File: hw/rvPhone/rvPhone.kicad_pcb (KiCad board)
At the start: 4 copper layers, 126 x 68 mm, 262 parts, among them J1 USB_OTG, J2 BATT, J201 Modem, J202 SIM_Card, J203 Motor, J204 Micro_SD_Card_Det, J205 Prog, J206 Expansion, J207 Camera, J3 +5V, J301 iMX8, J302 Micro_SD_Card_Det, J303 Spacer, J4 SJ-3571N, J401 Display, J402 Spacer, J403 Spacer, J5 SPEAKER, SW1 RESET, SW2 WAKE, SW201 ESP32_RST, SW202 MODEM_RST, SW301 iMX8_ALT_BOOT, SW302 iMX8_RST, SW303 iMX8_PWR, U1 BQ25895, U10 74HC595, U11 ICS-43434, U12 MAX98357A, U13 MAX98357A, U14 SN74LVC1G04DCK, U15 SN74LVC1G3157DCK, U16 SN74LVC2G07DCK, U2 TPS62293, U201 ESP32-WROOM, U202 SN74CBTLV3125RGY, U203 TXB0104RGY, U204 TXB0104RGY, U205 DRV2605LDGS, U206 LSM9DS1, U207 FT230XQ, U208 TMUX154ERSW, U3 TPS630250, U4 FE310-G002, U401 FAN5333BSX, U402 SN74LVC3G06DCU, U403 BT817Q, U404 IS25LP128-JKLE, U405 DS90C185, U406 TS3DV520ERUA, U407 TMUX1574RSV, U5 IS25LP128-JKLE, U6 TMUX1574RSV, U7 74HC00, U8 74HC00, U9 74HC595, X1 SiT1533, Y1 16MHz, Y401 12MHz

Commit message: HW REV 3.0
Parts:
- removed the C42 at (111.3, 135.4)
- removed the C43 at (108.0, 134.8)
- removed the C44 at (108.0, 132.8)
- removed the R31 at (163.8, 106.3)
- removed TP1: BQ_INT, TestPoint:TestPoint_Pad_D1.5mm
- removed TP401: AUDIO, TestPoint:TestPoint_Pad_D1.5mm
- added C39: 0.1uF, Capacitor_SMD:C_0603_1608Metric, B.Cu at (218.2, 121.0)
- added C40: 0.1uF, Capacitor_SMD:C_0603_1608Metric, B.Cu at (218.2, 124.0)
- added C45: 0.1uF, Capacitor_SMD:C_0603_1608Metric, B.Cu at (230.0, 117.0)
- added C50: 10uF, Capacitor_SMD:C_0603_1608Metric, F.Cu at (117.2, 136.6)
- added C51: 22uF, Capacitor_SMD:C_0805_2012Metric, F.Cu at (109.2, 135.4)
- added C52: 22uF, Capacitor_SMD:C_0805_2012Metric, F.Cu at (107.2, 135.4)
- added C53: 10uF, Capacitor_SMD:C_0603_1608Metric, F.Cu at (112.5, 133.4)
- added C54: 10uF, Capacitor_SMD:C_0603_1608Metric, F.Cu at (111.0, 133.4)
- added C9: 10uF, Capacitor_SMD:C_0603_1608Metric, F.Cu at (130.6, 122.7)
- added D2: LED, LED_SMD:LED_0603_1608Metric, B.Cu at (117.7, 138.3)
- added J6: Ext Audio, Connector_Molex:Molex_SlimStack_54722-0164_2x08_P0.50mm_Vertical, F.Cu at (228.2, 122.7)
- added JP1: AUDIO PWR, Jumper:SolderJumper-3_P1.3mm_Open_RoundedPad1.0x1.5mm, B.Cu at (162.1, 134.1)
- added U15: MAX14689A, footprints:TDFN-10-1EP_2x2.5mm_P0.4mm_EP1.3x1.4mm_ThermalVias, F.Cu at (219.4, 121.0)
- added U16: MAX14689A, footprints:TDFN-10-1EP_2x2.5mm_P0.4mm_EP1.3x1.4mm_ThermalVias, F.Cu at (219.4, 124.0)
- added U19: 74LVC1G02, footprints:Texas_R-PDSO-G5, F.Cu at (230.0, 117.0)
- C1: value 47nF -> 1uF
- C2: value 10uF -> 47nF
- C3: value 10uF -> 4.7uF
- C4: value 1uF -> 10uF
- C5: value 4.7uF -> 10uF
- D1: value LED -> B5817WS; footprint LED_SMD:LED_0603_1608Metric -> footprints:D_SOD-323; moved to F.Cu
- J303: value Spacer -> Console; footprint footprints:Spacer -> Connector_FFC-FPC:Hirose_FH12-6S-0.5SH_1x06-1MP_P0.50mm_Horizontal; moved to B.Cu
- L1: footprint Inductor_SMD:L_Vishay_IHLP-1616 -> Inductor_SMD:L_Vishay_IHLP-2525
- R2: value 10K -> 5.23K
- R26: value 2.2K -> 100K
- R27: value 255K -> 210K
- R3: value 2.2K -> 30.1K; moved to F.Cu
- R4: value 10K -> 2.2K; moved to B.Cu
- U18: renamed from U15; value SN74LVC1G3157DCK -> TMUX1119DCK
- moved J303 47.2 mm to (137.4, 76.9)
- moved R11 33.5 mm to (200.1, 138.1), turned to 270 degrees
- moved R26 20.4 mm to (226.8, 118.2), turned to 180 degrees
- moved SW2 16.6 mm to (150.2, 138.2)
- moved C7 12.6 mm to (120.2, 124.7), turned to 0 degrees
- moved L2 11.8 mm to (133.8, 124.3)
- moved U2 11.8 mm to (129.8, 124.7)
- moved C5 11.2 mm to (114.8, 122.0), turned to 270 degrees
- moved SW303 10.8 mm to (129.4, 136.2)
- moved SW302 10.8 mm to (133.2, 136.2)
- moved R32 9.79 mm to (205.1, 119.2)
- moved C41 9.62 mm to (221.2, 136.8)
- moved C42 9.62 mm to (221.2, 128.4)
- moved R28 9.62 mm to (225.8, 136.8)
- moved R29 9.62 mm to (225.8, 128.4)
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- renumbered C9 to C10, C10 to C11, C11 to C12, C12 to C13, C13 to C14, C45 to C28, C28 to C29, C29 to C30, C30 to C31, C31 to C32, C32 to C33, C33 to C34, C34 to C35, C35 to C36, C36 to C37, C37 to C38, C38 to C41, C39 to C42, C40 to C43, C41 to C44, C14 to C55, R16 to R15, R15 to R16, R32 to R31, R33 to R32, U9 to U10, U10 to U11, U11 to U12, U12 to U13, U13 to U14, U14 to U17, U16 to U6, U6 to U7, U7 to U8, U8 to U9
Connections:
- net /HP_SWITCH renamed /~HP_DET
- net /periph/ESP32.EN renamed /periph/ESP32_EN
- net /periph/ESP32.PCM.CLK renamed /periph/ESP32_PCM_CLK
- net /periph/ESP32.PCM.DI renamed /periph/ESP32_PCM_DI
- net /periph/ESP32.PCM.DO renamed /periph/ESP32_PCM_DO
- net /periph/ESP32.PCM.SYNC renamed /periph/ESP32_PCM_SYNC
- net /periph/ESP32.U2.DTR renamed /periph/ESP32_UART2_DTR
- net /periph/ESP32.U2.RI renamed /periph/ESP32_UART2_RI
- net /periph/ESP32.U2.RXD renamed /periph/ESP32_UART2_RXD
- net /periph/ESP32.U2.TXD renamed /periph/ESP32_UART2_TXD
- net /periph/ESP32.VSPI.MISO renamed /periph/ESP32_VSPI_MISO
- net /periph/ESP32.VSPI.MOSI renamed /periph/ESP32_VSPI_MOSI
- net /periph/ESP32.VSPI.SCK renamed /periph/ESP32_VSPI_SCK
- net /periph/ESP32.VSPI.SS0 renamed /periph/ESP32_VSPI_SS0
- net /periph/Modem.PCM.CLK renamed /periph/PCM_CLK
- net /periph/Modem.PCM.DI renamed /periph/PCM_DI
- net /periph/Modem.PCM.DO renamed /periph/PCM_DO
- net /periph/Modem.PCM.SYNC renamed /periph/PCM_SYNC
- net /periph/Quectel.UART.DTR renamed /periph/Quectel_UART_DTR
- net /periph/Quectel.UART.RI renamed /periph/Quectel_UART_RI
- net /periph/Quectel.UART.RXD renamed /periph/Quectel_UART_RXD
- net /periph/Quectel.UART.TXD renamed /periph/Quectel_UART_TXD
- net /periph/SIMCom.UART.DTR renamed /periph/SIMCom_UART_DTR
- net /periph/SIMCom.UART.RI renamed /periph/SIMCom_UART_RI
- net /periph/SIMCom.UART.TXD renamed /periph/SIMCom_UART_TXD
- C1 pad 1: Net-(C1-Pad1) -> VBUS
- C1 pad 2: Net-(C1-Pad2) -> GND
- C2 pad 1: +VSYS -> /BQ_SW
- C2 pad 2: GND -> Net-(C2-Pad2)
- C3 pad 1: +VSYS -> Net-(C3-Pad1)
- C35 pad 1: +VSYS -> VDDA
- C36 pad 1: +VSYS -> VDDA
- C37 pad 1: +VSYS -> VDDA
- C38 pad 1: +VSYS -> VDDA
- C4 pad 1: VBUS -> +VSYS
- C41 pad 2: Net-(C38-Pad2) -> /HP_R
- C42 pad 2: Net-(C39-Pad2) -> /HP_L
- C44 pad 1: +VSYS -> VDDA
- C5 pad 1: Net-(C5-Pad1) -> +VSYS
- C7 pad 1: +VSYS -> Net-(C6-Pad1)
- C8 pad 1: +1V8 -> +VSYS
- D1 pad 1: Net-(D1-Pad1) -> /BQ_PMID
- D1 pad 2: +VSYS -> /BQ_SW
- J206 pad 10: TMUX.I2C0.SCL -> Net-(J206-Pad10)
- J206 pad 12: GND -> TMUX.I2C0.SDA
- J206 pad 14: TMUX.GPIO1 -> TMUX.I2C0.SCL
- J206 pad 16: TMUX.GPIO0 -> GND
- J206 pad 2: +VSYS -> VDDA
- J206 pad 3: GND -> +3V3
- J206 pad 4: +VSYS -> VDDA
- J206 pad 8: TMUX.I2C0.SDA -> Net-(J206-Pad8)
- J207 pad 1: TMUX.I2C0.SCL -> +3V3
- J207 pad 10: GND -> BT81X.GPIO0
- J207 pad 11: +VSYS -> GND
- J207 pad 12: GND -> TMUX.I2C0.SDA
- J207 pad 13: +VSYS -> Net-(J207-Pad13)
- J207 pad 14: GND -> TMUX.I2C0.SCL
- J207 pad 15: GND -> Net-(J207-Pad15)
- J207 pad 16: +3V3 -> GND
- J207 pad 2: SPI1.SCK -> +VSYS
- J207 pad 3: TMUX.I2C0.SDA -> +3V3
- J207 pad 4: SPI1.MISO -> +VSYS
- J207 pad 5: SPI1.SS2 -> SPI1.MOSI
- J207 pad 6: SPI1.MOSI -> GND
- J207 pad 7: GND -> SPI1.MISO
- J207 pad 8: BT81X.GPIO0 -> SPI1.SS2
- J207 pad 9: GND -> SPI1.SCK
- J301 pad 111: Net-(J301-Pad111) -> /exp/UART3_TX
- J301 pad 117: Net-(J301-Pad117) -> /exp/UART3_RX
- J303 pad 1: GND -> Net-(J303-Pad1)
- J4 pad 4: /SPK_L+ -> Net-(J4-Pad4)
- J4 pad 5: /SPK_L_HP+ -> Net-(J4-Pad5)
- J4 pad 6: Net-(C39-Pad2) -> Net-(J4-Pad6)
- J4 pad 7: /SPK_R+ -> Net-(J4-Pad7)
- J4 pad 8: /SPK_R_HP_+ -> Net-(J4-Pad8)
- J4 pad 9: Net-(C38-Pad2) -> Net-(J4-Pad9)
- L1 pad 1: Net-(C1-Pad1) -> /BQ_SW
- R15 pad 2: GND -> +3V3
- R2 pad 1: Net-(C5-Pad1) -> Net-(C3-Pad1)
- R26 pad 1: Net-(R26-Pad1) -> BT81X.GPIO2
- R26 pad 2: /SPK_EN -> +3V3
- R3 pad 1: Net-(R3-Pad1) -> Net-(R2-Pad2)
- R3 pad 2: Net-(D1-Pad1) -> GND
- R31 pad 1: +VSYS -> VDDA
- R31 pad 2: Net-(R32-Pad2) -> Net-(R31-Pad2)
- R32 pad 1: Net-(R33-Pad1) -> Net-(R32-Pad1)
- R4 pad 1: Net-(R2-Pad2) -> Net-(R4-Pad1)
- R4 pad 2: GND -> Net-(D2-Pad1)
- U1 pad 19: Net-(C1-Pad1) -> /BQ_SW
- U1 pad 20: Net-(C1-Pad1) -> /BQ_SW
- U1 pad 21: Net-(C1-Pad2) -> Net-(C2-Pad2)
- U1 pad 22: Net-(C5-Pad1) -> Net-(C3-Pad1)
- U1 pad 4: Net-(R3-Pad1) -> Net-(R4-Pad1)
- U1 pad 7: /BQ_INT -> BQ.INT
- U13 pad 10: /SPK_L- -> /AUDIO_OUT_L-
- U13 pad 4: Net-(R26-Pad1) -> /SPK_EN
- U13 pad 7: +VSYS -> VDDA
- U13 pad 8: +VSYS -> VDDA
- U13 pad 9: /SPK_L_HP+ -> /AUDIO_OUT_L+
- U14 pad 10: /SPK_R- -> /AUDIO_OUT_R-
- U14 pad 7: +VSYS -> VDDA
- U14 pad 8: +VSYS -> VDDA
- U14 pad 9: /SPK_R_HP_+ -> /AUDIO_OUT_R+
- U18 pad 1: Net-(R32-Pad2) -> /SPK_GAIN_SEL
- U18 pad 2: GND -> VDDA
- U18 pad 3: Net-(R33-Pad1) -> GND
- U18 pad 4: /SPK_GAIN -> Net-(R32-Pad1)
- U18 pad 5: +VSYS -> /SPK_GAIN
- U18 pad 6: /SPK_GAIN_SEL -> Net-(R31-Pad2)
- U201 pad 10: Net-(U201-Pad10) -> BQ.INT
- U403 pad 26: /disp/BT81X_AUDIO -> BT81X.AUDIO
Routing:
- net BQ.INT: track 0.00 -> 181.9 mm, vias 0 -> 4
- net BT81X.AUDIO: track 0.00 -> 83.4 mm, vias 0 -> 2
- net GND: track 502.9 -> 570.3 mm, vias 632 -> 597
- net BT81X.GPIO2: track 74.4 -> 123.0 mm, vias 5 -> 7
- net /exp/POWER: track 38.2 -> 81.1 mm, vias 1 -> 2
- net /SPK_EN: track 41.0 -> 81.4 mm, vias 4 -> 8
- net WAKE: track 117.8 -> 147.6 mm, vias 6 -> 7
- net /SPK_L+: track 9.98 -> 35.4 mm, vias 0 -> 2
- net /exp/RESET: track 61.1 -> 83.2 mm, vias 1 -> 2
- net VDDA: track 0.00 -> 19.6 mm, vias 0 -> 13
- net /exp/ALT_BOOT: track 57.4 -> 76.5 mm, vias 1 -> 2
- net TMUX.GPIO0: track 90.1 -> 71.3 mm, vias 5 -> 3
- net Net-(U201-Pad4): track 18.8 -> 0.00 mm
- net Net-(U201-Pad5): track 17.0 -> 0.00 mm
- net /~HP_DET: track 19.7 -> 35.7 mm, vias 2 -> 4
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- added copper zone on PWR, net /BQ_PMID
- added copper zone on F.Cu, net /BQ_SW
- added copper zone on F.Cu, net VDDA
- added copper zone on PWR, net VDDA
- removed copper zone on F.Cu, net /SPK_L_HP+
- removed copper zone on F.Cu, net /SPK_R_HP_+
- removed copper zone on F.Cu, net Net-(C1-Pad1)
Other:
- outline, holes or cut-outs redrawn

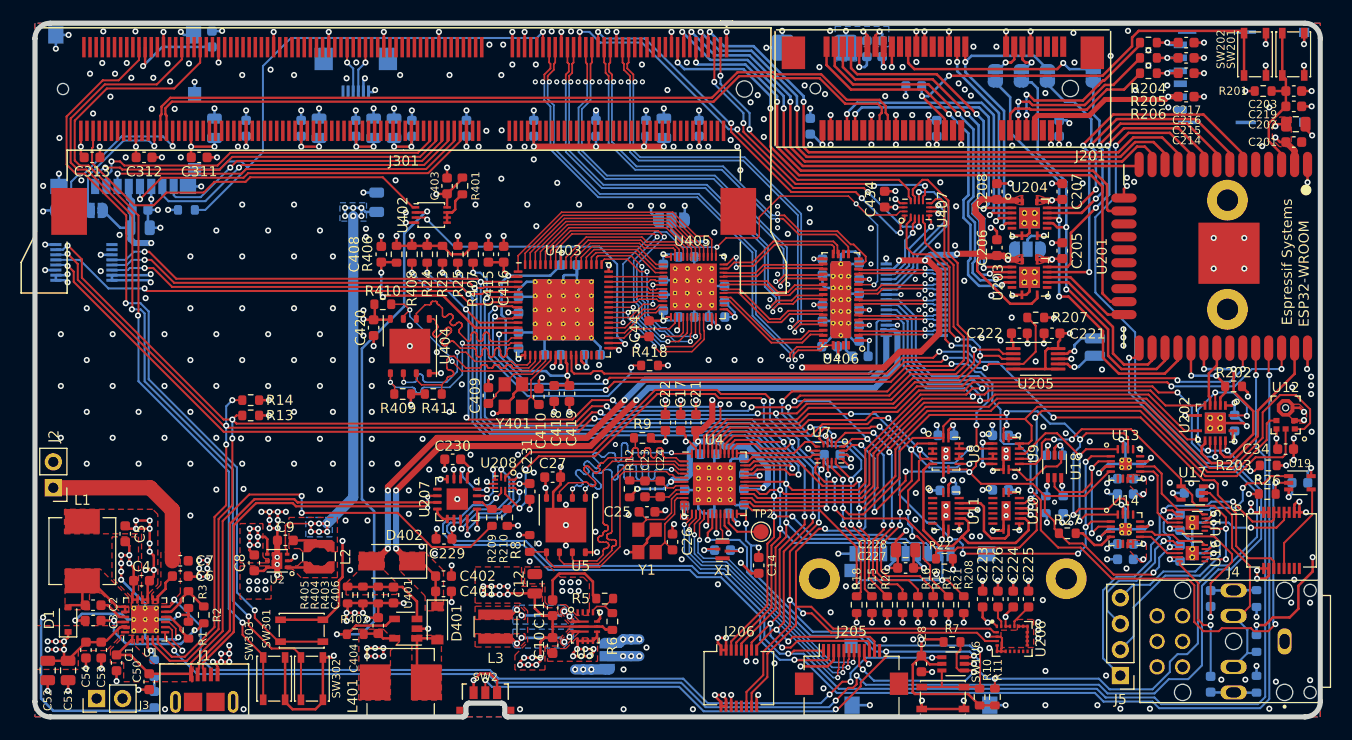
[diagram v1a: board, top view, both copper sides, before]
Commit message: added pull-up pull-dn resistors; fixed input power;
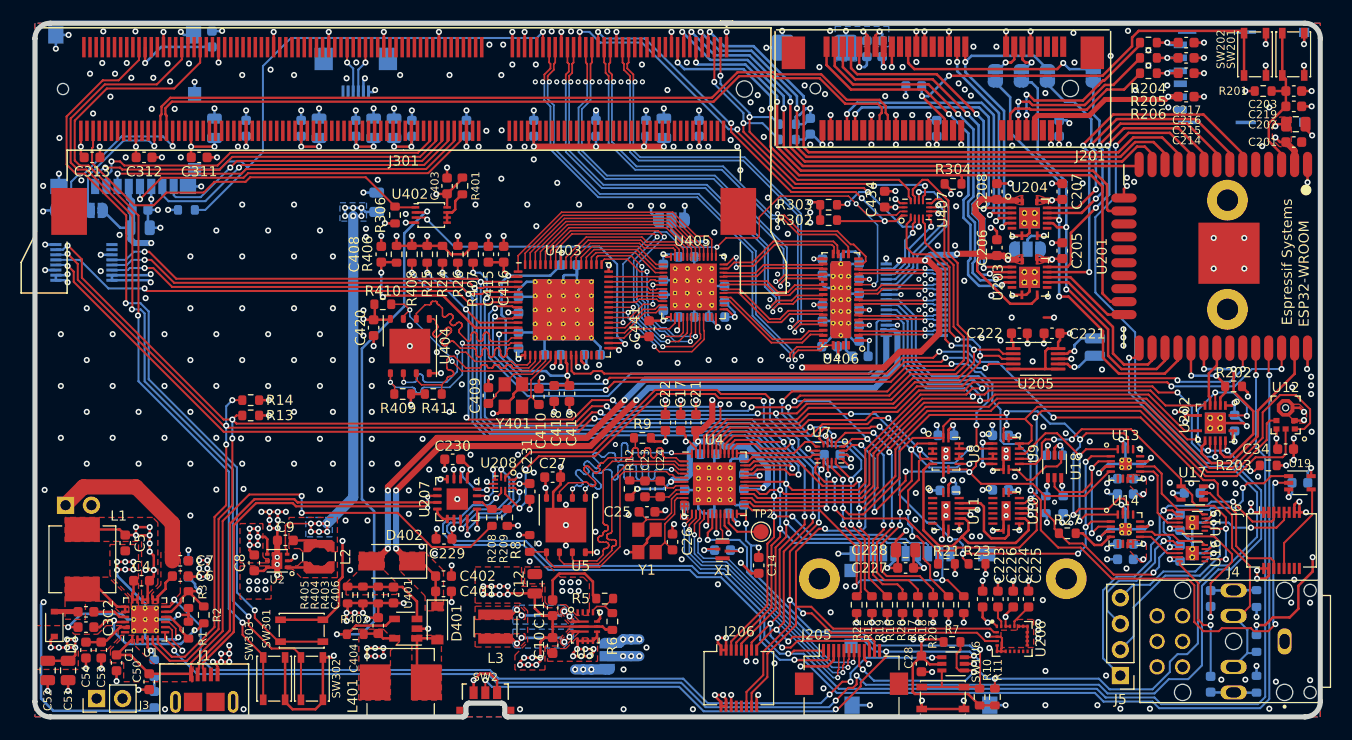
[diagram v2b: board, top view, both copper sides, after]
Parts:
- removed the R207 at (204.1, 100.8)
- removed the R26 at (226.8, 118.2)
- removed R418: 100K, Resistor_SMD:R_0603_1608Metric
- added R23: 100K, Resistor_SMD:R_0603_1608Metric, F.Cu at (198.3, 125.0)
- added R302: 10K, Resistor_SMD:R_0603_1608Metric, F.Cu at (183.8, 91.3)
- added R303: 10K, Resistor_SMD:R_0603_1608Metric, F.Cu at (183.8, 89.8)
- added R304: 47K, Resistor_SMD:R_0603_1608Metric, F.Cu at (196.0, 87.8)
- added R305: 47K, Resistor_SMD:R_0603_1608Metric, B.Cu at (179.8, 83.4)
- added R306: 100K, Resistor_SMD:R_0603_1608Metric, F.Cu at (141.3, 90.8)
- added R307: 100K, Resistor_SMD:R_0603_1608Metric, B.Cu at (179.8, 81.9)
- added R33: 10K, Resistor_SMD:R_0603_1608Metric, B.Cu at (121.0, 125.5)
- C14: value 10nF -> 0.01uF
- C2: value 47nF -> 0.047uF
- J2: moved to B.Cu
- R15, R301: value 100K -> 47K
- moved J2 2.09 mm to (109.0, 119.2), turned to 270 degrees
- moved D1 1.42 mm to (107.9, 130.9)
- moved C2 0.96 mm to (111.0, 129.7)
- moved C3 0.96 mm to (111.0, 131.2)
- moved C5 0.90 mm to (114.8, 123.0)
- moved L1 0.80 mm to (110.7, 124.5)
- moved R21 0.54 mm to (195.3, 125.0)
- renumbered R21 to R18, R20 to R19, R19 to R20, R208 to R207, R209 to R208, R210 to R209, R22 to R21, R18 to R22, R23 to R24, R24 to R25, R25 to R26
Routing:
- net GND: track 570.3 -> 578.1 mm, vias 597 -> 604
- net BT81X.GPIO3: track 63.5 -> 57.2 mm
- net +VSYS: track 120.9 -> 126.1 mm
- net +3V3: track 238.2 -> 242.7 mm, vias 88 -> 89
- net iMX8.GPIO5.IO28: track 31.1 -> 35.3 mm
- net iMX8.I2C3.SDA: track 43.7 -> 47.3 mm, vias 4 -> 5
- net iMX8.GPIO5.IO29: track 28.7 -> 31.8 mm
- net iMX8.I2C3.SCL: track 41.7 -> 44.7 mm
- net Net-(R2-Pad2): track 5.43 -> 8.25 mm, vias 0 -> 1
- net /BQ_SW: track 10.00 -> 7.19 mm
- net BT81X.GPIO1: track 55.2 -> 53.6 mm, vias 2 -> 1
- net /SPK_SD: track 51.2 -> 52.5 mm
- net /BQ_PMID: track 18.0 -> 16.7 mm
- net Net-(C6-Pad1): track 20.9 -> 19.8 mm
- net Net-(U405-Pad23): track 1.08 -> 0.00 mm, vias 1 -> 0
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
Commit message: REV3.1:  - fixed audio  - added spacers  - UART is routed through audio mux instead of I2C  - proper display connector alignment
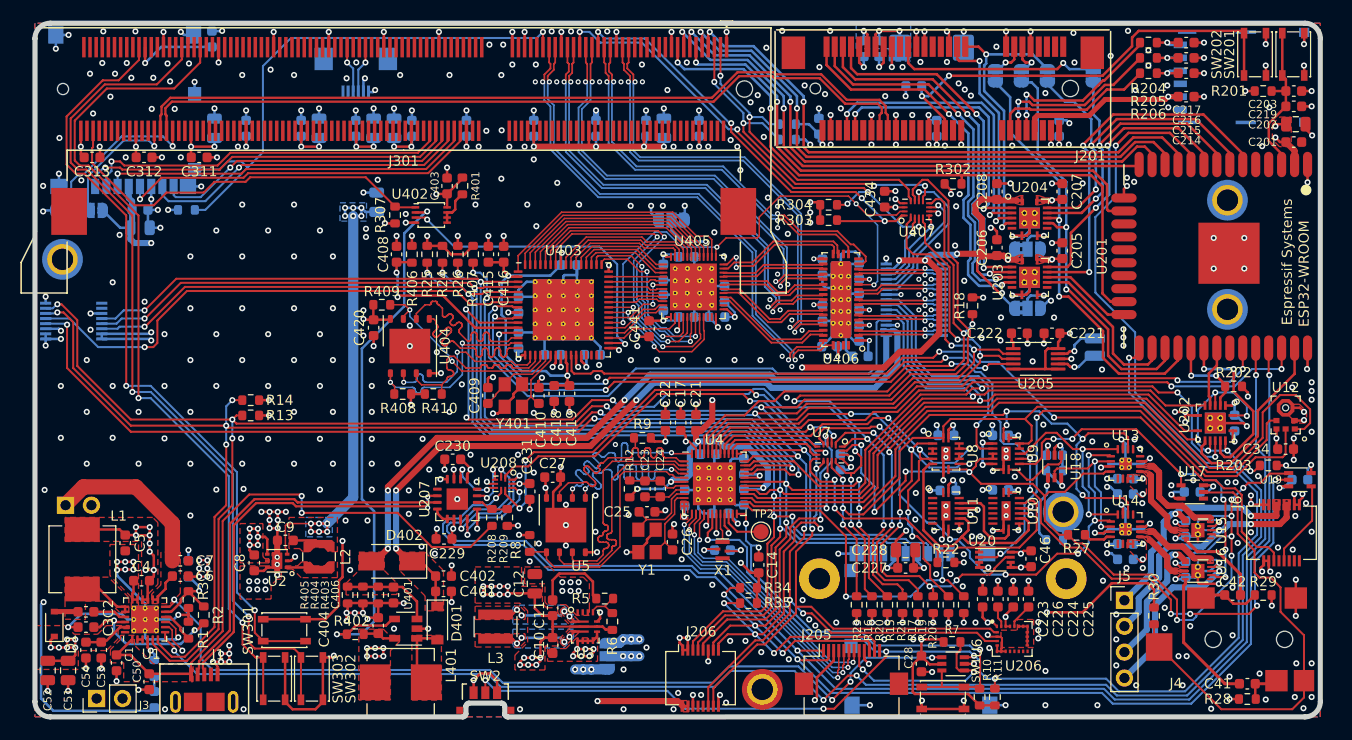
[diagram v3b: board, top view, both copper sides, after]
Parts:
- removed the R408 at (142.9, 94.7)
- added C46: 0.1uF, Capacitor_SMD:C_0603_1608Metric, F.Cu at (203.7, 124.5)
- added J208: Spacer, footprints:Spacer_small, F.Cu at (177.3, 137.3)
- added J209: Spacer, footprints:Spacer_small, B.Cu at (108.7, 95.2)
- added J404: Spacer, footprints:Spacer_small, B.Cu at (206.8, 119.9)
- added JP202: SIMCom_EN, Jumper:SolderJumper-3_P1.3mm_Bridged2Bar12_RoundedPad1.0x1.5mm, B.Cu at (203.3, 94.2)
- added R34: 100K, Resistor_SMD:R_0603_1608Metric, F.Cu at (175.9, 127.3)
- added R35: 100K, Resistor_SMD:R_0603_1608Metric, F.Cu at (175.9, 128.8)
- added U20: SN74LVC2G66DCU, Package_SO:VSSOP-8_2.3x2mm_P0.5mm, F.Cu at (200.1, 124.6)
- C41, C42, R28, R29, R30: moved to F.Cu
- J4: value SJ-3571N -> AudioJack; footprint footprints:SJ-3571N -> footprints:35RASMT4BHNTRX
- J402, J403: footprint footprints:Spacer -> footprints:Spacer_small
- JP201: value SIMCom_EN -> PCM_EN; footprint Jumper:SolderJumper-3_P1.3mm_Open_RoundedPad1.0x1.5mm -> Jumper:SolderJumper-3_P1.3mm_Bridged2Bar12_RoundedPad1.0x1.5mm
- JP402: footprint Jumper:SolderJumper-3_P1.3mm_Open_RoundedPad1.0x1.5mm -> Jumper:SolderJumper-3_P1.3mm_Bridged2Bar12_RoundedPad1.0x1.5mm
- R16: renamed from R15; value 47K -> 100K
- R306: renamed from R305; value 47K -> 100K
- R32: value 50K -> 0R
- moved R18 25.3 mm to (197.9, 99.7), turned to 270 degrees
- moved C218 11.5 mm to (193.9, 74.4), turned to 0 degrees
- moved R30 10.4 mm to (215.7, 130.1)
- moved J4 8.50 mm to (232.0, 132.4)
- moved J5 7.39 mm to (212.8, 128.6), turned to 0 degrees
- moved J207 5.84 mm to (109.8, 101.2)
- moved JP201 5.80 mm to (203.3, 100.0), turned to 0 degrees
- moved J206 3.75 mm to (171.2, 136.2)
- moved C41 3.60 mm to (224.8, 136.8), turned to 180 degrees
- moved R32 3.55 mm to (205.9, 122.7), turned to 0 degrees
- moved R31 3.46 mm to (205.9, 115.8), turned to 180 degrees
- moved C42 2.18 mm to (223.4, 128.1), turned to 0 degrees
- moved U16 1.83 mm to (220.0, 125.7)
- moved R28 1.71 mm to (224.8, 138.2), turned to 180 degrees
- moved SW301 1.70 mm to (130.4, 131.5)
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- renumbered JP202 to JP203, JP203 to JP204, JP204 to JP205, JP205 to JP206, R16 to R15, R23 to R18, R18 to R19, R19 to R20, R20 to R21, R21 to R22, R22 to R23, R304 to R302, R302 to R303, R303 to R304, R307 to R305, R306 to R307, R409 to R408, R410 to R409, R411 to R410
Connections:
- net BT81X.CTP.INT renamed Net-(U403-Pad30)
- net BT81X.CTP.RST renamed Net-(U403-Pad29)
- net BT81X.CTP.SCL renamed Net-(U403-Pad31)
- net BT81X.CTP.SDA renamed Net-(U403-Pad32)
- net TMUX.GPIO0 renamed CTP.RST
- C221 pad 1: GND -> +3V3
- C221 pad 2: +3V3 -> GND
- C51 pad 1: /BQ_PMID -> +5V
- C52 pad 1: /BQ_PMID -> +5V
- C53 pad 1: /BQ_PMID -> +5V
- C54 pad 1: /BQ_PMID -> +5V
- D1 pad 1: /BQ_PMID -> +5V
- J206 pad 12: TMUX.I2C0.SDA -> I2C0.SDA
- J206 pad 14: TMUX.I2C0.SCL -> I2C0.SCL
- J206 pad 2: VDDA -> +5V
- J206 pad 4: VDDA -> +5V
- J207 pad 12: TMUX.I2C0.SDA -> I2C0.SDA
- J207 pad 14: TMUX.I2C0.SCL -> I2C0.SCL
- J3 pad 1: /BQ_PMID -> +5V
- JP1 pad 3: /BQ_PMID -> +5V
- JP201 pad 1: GND -> +1V8
- JP201 pad 3: +1V8 -> GND
- JP402 pad 1: +1V8 -> GND
- JP402 pad 3: GND -> +1V8
- R13 pad 2: TMUX.I2C0.SCL -> I2C0.SCL
- R14 pad 2: TMUX.I2C0.SDA -> I2C0.SDA
- R15 pad 2: GND -> +3V3
- R16 pad 1: TMUX.GPIO1 -> BT81X.INT
- R18 pad 2: /SPK_SD -> GPIO_23
- R22 pad 2: /MIC_SD -> /SD_OUT
- R305 pad 1: GND -> +3V3
- R306 pad 1: +3V3 -> GND
- U1 pad 23: /BQ_PMID -> +5V
- U1 pad 5: TMUX.I2C0.SCL -> I2C0.SCL
- U1 pad 6: TMUX.I2C0.SDA -> I2C0.SDA
- U10 pad 14: /MIC_SD -> /SD_OUT
- U11 pad 9: /SPK_SD -> /SD_IN
- U13 pad 1: /SPK_SD -> /SD_IN
- U14 pad 1: /SPK_SD -> /SD_IN
- U203 pad 8: +1V8 -> Net-(JP201-Pad2)
- U204 pad 8: Net-(JP201-Pad2) -> Net-(JP202-Pad2)
- U205 pad 2: TMUX.I2C0.SCL -> I2C0.SCL
- U205 pad 3: TMUX.I2C0.SDA -> I2C0.SDA
- U206 pad 2: TMUX.I2C0.SCL -> I2C0.SCL
- U206 pad 4: TMUX.I2C0.SDA -> I2C0.SDA
- U4 pad 36: GPIO_12 -> I2C0.SDA
- U4 pad 37: GPIO_13 -> I2C0.SCL
- U4 pad 38: UART0.RXD -> GPIO_16
- U4 pad 39: UART0.TXD -> GPIO_17
- U403 pad 11: GPIO_23 -> BT81X.INT
- U407 pad 1: TMUX.I2C0.SCL -> I2C0.SCL
- U407 pad 4: TMUX.I2C0.SDA -> I2C0.SDA
- U407 pad 8: TMUX.GPIO1 -> GPIO_23
- U7 pad 12: TMUX.GPIO1 -> BT81X.INT
- U7 pad 3: TMUX.I2C0.SCL -> UART0.TXD
- U7 pad 4: /SPK_SD -> /SD_IN
- U7 pad 5: GPIO_13 -> GPIO_17
- U7 pad 7: GPIO_12 -> GPIO_16
- U7 pad 8: /MIC_SD -> /SD_OUT
- U7 pad 9: TMUX.I2C0.SDA -> UART0.RXD
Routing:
- net I2C0.SCL: track 0.00 -> 219.2 mm, vias 0 -> 9
- net TMUX.I2C0.SCL: track 219.0 -> 0.00 mm, vias 10 -> 0
- net I2C0.SDA: track 0.00 -> 216.8 mm, vias 0 -> 12
- net TMUX.I2C0.SDA: track 210.4 -> 0.00 mm, vias 13 -> 0
- net BT81X.INT: track 0.00 -> 78.1 mm, vias 0 -> 6
- net TMUX.GPIO1: track 65.4 -> 0.00 mm, vias 3 -> 0
- net /SPK_SD: track 52.5 -> 0.00 mm, vias 6 -> 0
- net /SD_IN: track 0.00 -> 52.4 mm, vias 0 -> 6
- net /SD_OUT: track 0.00 -> 36.1 mm, vias 0 -> 2
- net /MIC_SD: track 74.5 -> 48.0 mm, vias 4 -> 2
- net +5V: track 0.00 -> 25.8 mm, vias 0 -> 10
- net /HP_DET: track 22.4 -> 46.2 mm
- net /SPK_EN: track 81.4 -> 99.3 mm, vias 8 -> 12
- net /BQ_PMID: track 16.7 -> 0.00 mm, vias 9 -> 0
- net GND: track 578.1 -> 591.8 mm, vias 604 -> 636
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- added copper zone on F.Cu, net +5V
- added copper zone on PWR, net +5V
- added copper zone on F.Cu, net /AUDIO_OUT_L+
- added copper zone on F.Cu, net /AUDIO_OUT_L-
- added copper zone on F.Cu, net /AUDIO_OUT_R+
- added copper zone on F.Cu, net /AUDIO_OUT_R-
- added copper zone on F.Cu, net /HP_L
- added copper zone on F.Cu, net /SPK_L+
- added copper zone on F.Cu, net /SPK_L-
- added copper zone on F.Cu, net /SPK_R+
- removed copper zone on F.Cu, net /BQ_PMID
- removed copper zone on PWR, net /BQ_PMID
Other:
- outline, holes or cut-outs redrawn
- net class FE310_L removed
- net class PRIMARY added: clearance 0.2, trace_width 0.2, via_dia 0.6, via_drill 0.3
- net class USB removed
- net class USB2UART added: clearance 0.2, trace_width 0.2, via_dia 0.6, via_drill 0.3
